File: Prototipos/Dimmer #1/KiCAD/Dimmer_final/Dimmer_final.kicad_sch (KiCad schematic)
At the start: 27 parts, among them J2 Conn_01x02, K1 SRD-05VDC-SL-C, Q1 BC548B, Q2 BT137, U1 MOC3021M, U2 EL817

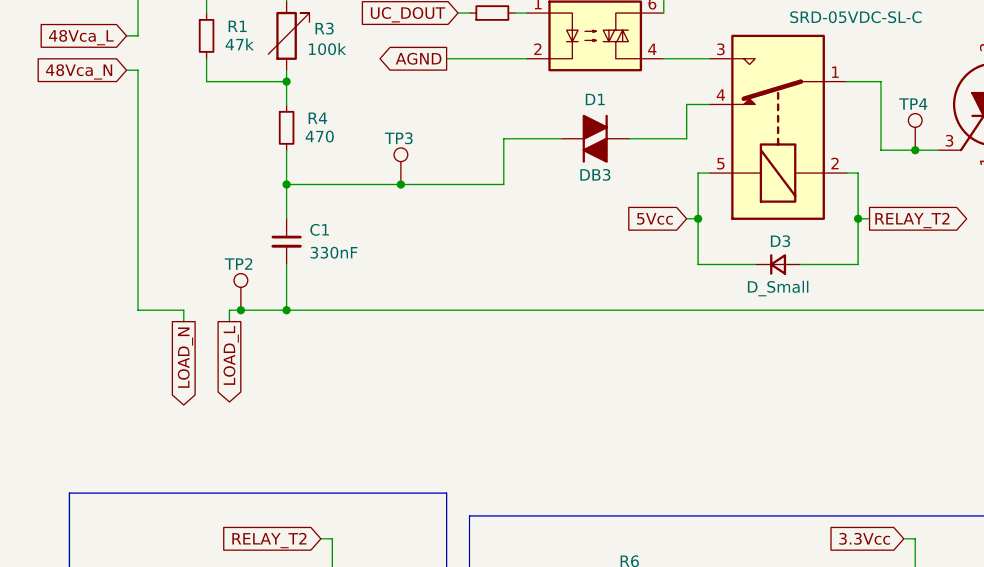
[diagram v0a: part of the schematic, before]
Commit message: Primeras modificaciones para constraints JLCPCB
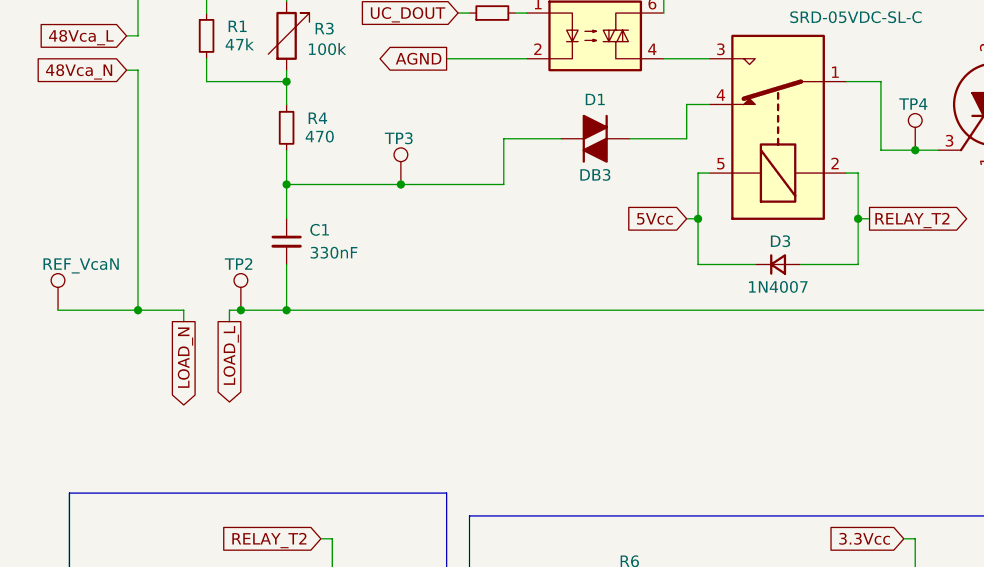
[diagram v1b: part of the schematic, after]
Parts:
- added REF_VcaN: TestPoint, TestPoint:TestPoint_Loop_D1.80mm_Drill1.0mm_Beaded, symbol Connector:TestPoint
- D3: value D_Small -> 1N4007
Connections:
- net 48Vca_N: now also REF_VcaN.1
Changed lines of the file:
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@@
+	)
+	(junction
+		(at 46.99 82.55)
+		(diameter 0)
+		(color 0 0 0 0)
 	)
 	(junction
@@
 	(wire
 		(pts
-			(xy 52.07 82.55) (xy 46.99 82.55)
-		)
-		(stroke
-			(width 0)
-			(type default)
-		)
-	)
-	(wire
-		(pts
 			(xy 58.42 82.55) (xy 63.5 82.55)
 		)
@@
 	(wire
 		(pts
+			(xy 38.1 82.55) (xy 46.99 82.55)
+		)
+		(stroke
+			(width 0)
+			(type default)
+		)
+	)
+	(wire
+		(pts
 			(xy 110.49 59.69) (xy 107.95 59.69)
 		)
@@
 		(pts
 			(xy 63.5 64.8245) (xy 63.5 68.58)
+		)
+		(stroke
+			(width 0)
+			(type default)
+		)
+	)
+	(wire
+		(pts
+			(xy 46.99 82.55) (xy 52.07 82.55)
 		)
 		(stroke
@@
 	)
 	(symbol
+		(lib_id "Connector:TestPoint")
+		(at 38.1 82.55 0)
+		(unit 1)
+		(exclude_from_sim no)
+		(in_bom yes)
+		(on_board yes)
+		(dnp no)
+		(property "Reference" "REF_VcaN"
+			(at 36.322 77.47 0)
+			(effects
+				(font
+					(size 1.27 1.27)
+				)
+				(justify left)
+			)
+		)
+		(property "Value" "TestPoint"
+			(at 31.75 79.502 0)
+			(effects
+				(font
+					(size 1.27 1.27)
+				)
+				(justify left)
+				(hide yes)
+			)
+		)
+		(property "Footprint" "TestPoint:TestPoint_Loop_D1.80mm_Drill1.0mm_Beaded"
+			(at 43.18 82.55 0)
+			(effects
+				(font
+					(size 1.27 1.27)
+				)
+				(hide yes)
+			)
+		)
+		(property "Datasheet" "~"
+			(at 43.18 82.55 0)
+			(effects
+				(font
+					(size 1.27 1.27)
+				)
+				(hide yes)
+			)
+		)
+		(property "Description" "test point"
+			(at 38.1 82.55 0)
+			(effects
+				(font
+					(size 1.27 1.27)
+				)
+				(hide yes)
+			)
+		)
+		(pin "1"
+		)
+		(instances
+			(project "Dimmer_final"
+				(path "/7934e872-2b7f-4f8f-a0b6-741d97320597"
+					(reference "REF_VcaN")
+					(unit 1)
+				)
+			)
+		)
+	)
+	(symbol
 		(lib_id "Device:R_Small")
 		(at 57.15 119.38 90)
@@
 			)
 		)
-		(property "Value" "D_Small"
+		(property "Value" "1N4007"
 			(at 118.11 80.01 0)
 			(effects

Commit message: Reversionado dimmer para fabricación industrial
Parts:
- C1, C2: footprint Capacitor_THT:C_Disc_D10.5mm_W5.0mm_P7.50mm -> Capacitor_THT:C_Disc_D4.7mm_W2.5mm_P5.00mm
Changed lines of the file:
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@@
 			)
 		)
-		(property "Footprint" "Capacitor_THT:C_Disc_D10.5mm_W5.0mm_P7.50mm"
+		(property "Footprint" "Capacitor_THT:C_Disc_D4.7mm_W2.5mm_P5.00mm"
 			(at 63.5 74.93 0)
 			(effects
@@
 			)
 		)
-		(property "Footprint" "Capacitor_THT:C_Disc_D10.5mm_W5.0mm_P7.50mm"
+		(property "Footprint" "Capacitor_THT:C_Disc_D4.7mm_W2.5mm_P5.00mm"
 			(at 154.94 69.85 0)
 			(effects

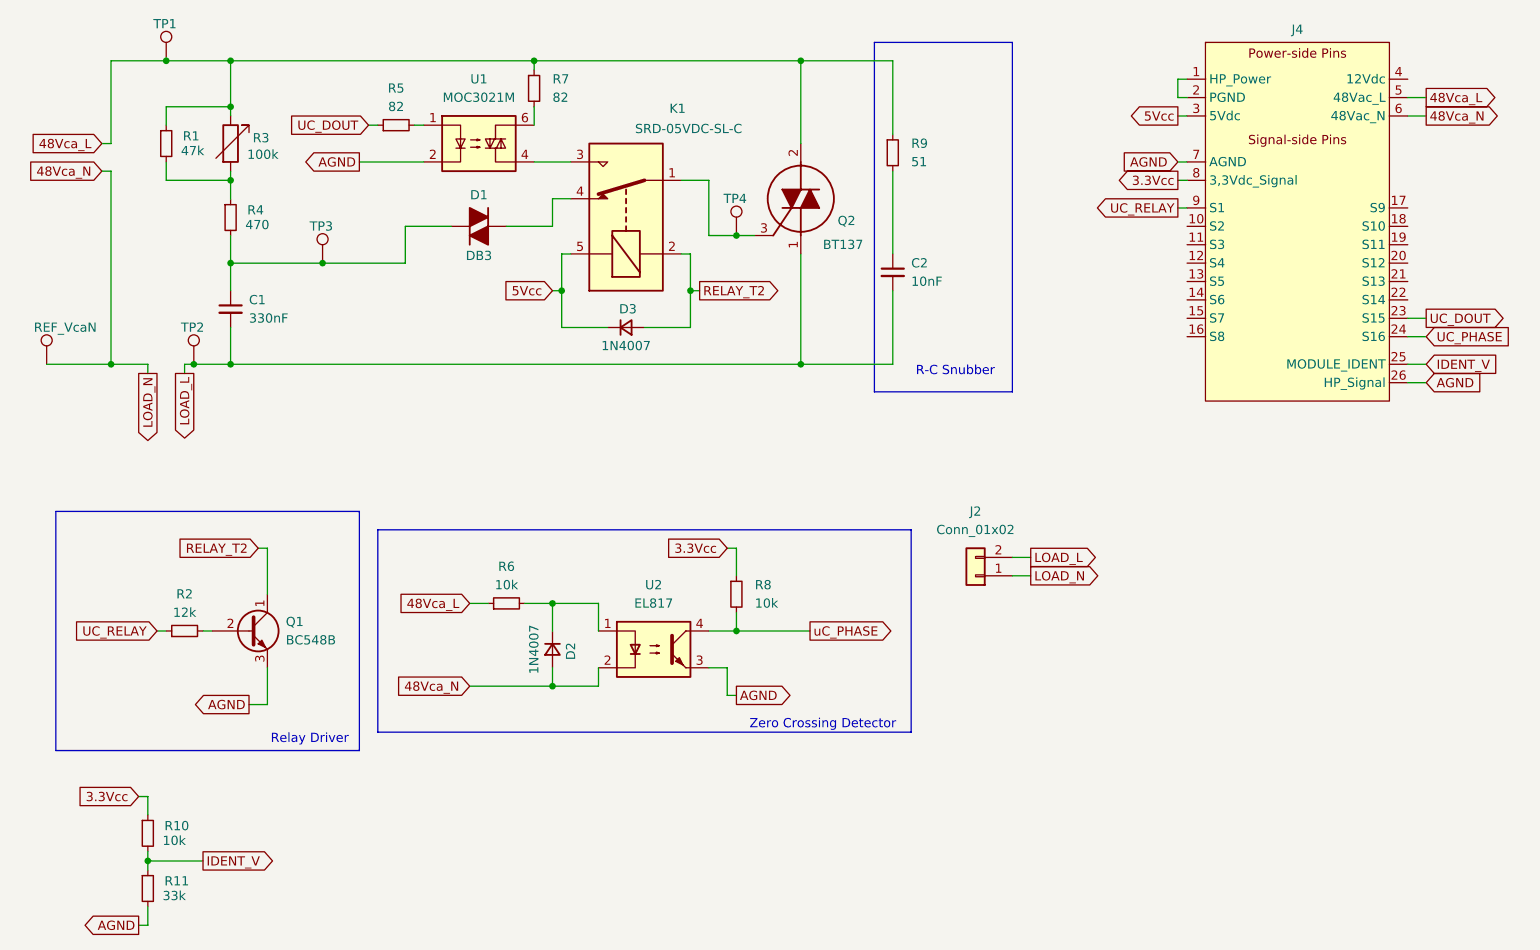
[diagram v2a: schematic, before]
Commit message: Agregar titulo de módulo y firma
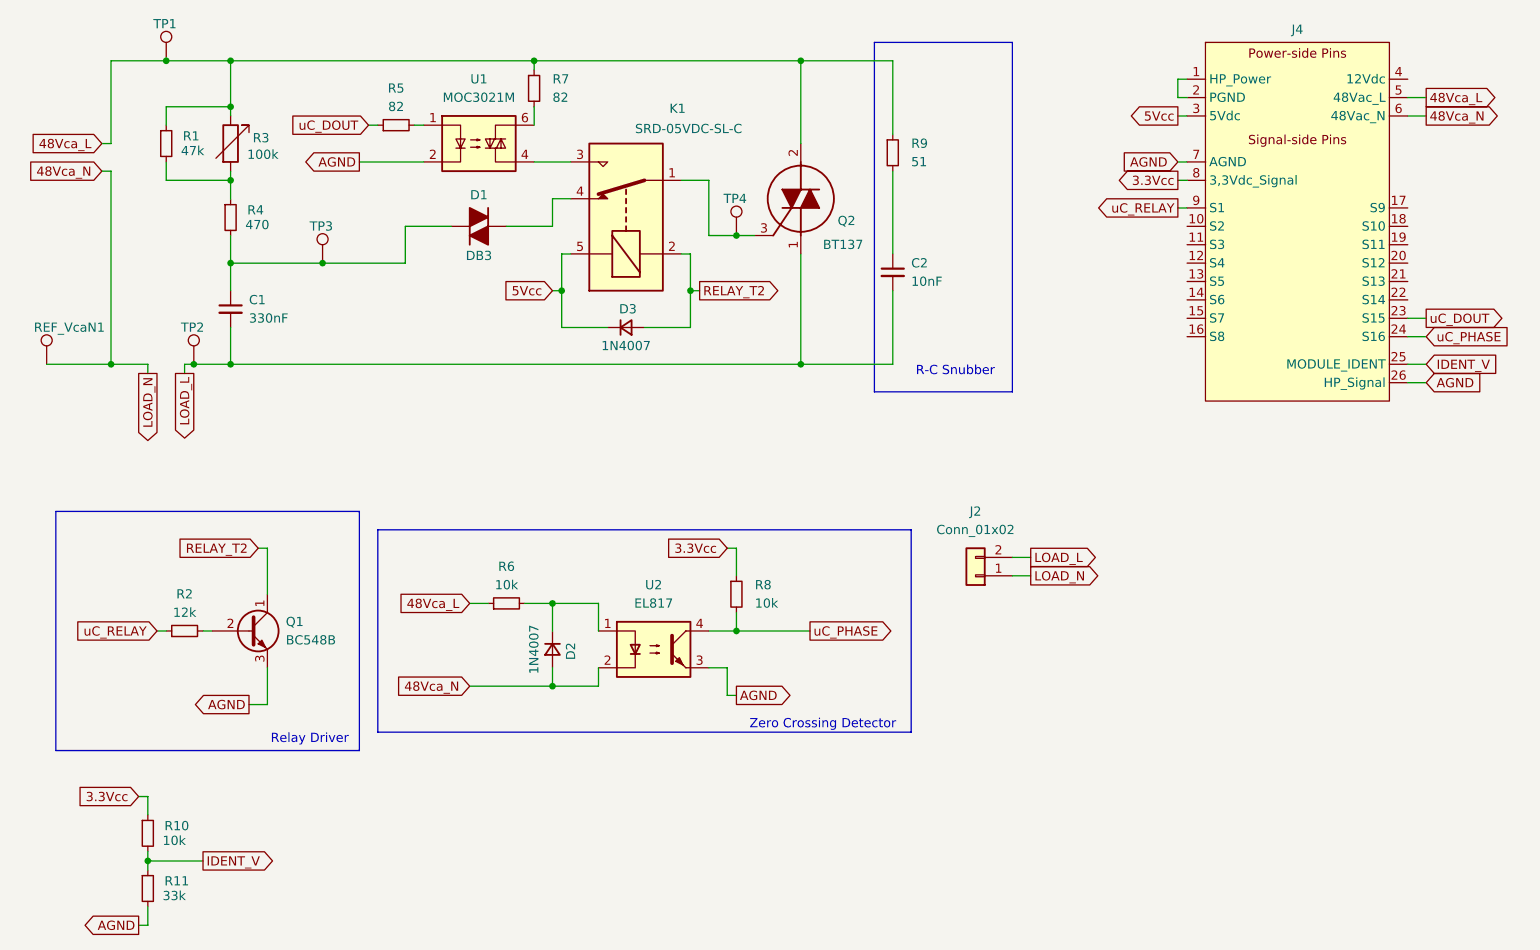
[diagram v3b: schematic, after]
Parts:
- renumbered REF_VcaN to REF_VcaN1
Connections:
- net UC_PHASE is gone; now on net uC_PHASE: J4.24 (S16)
- net UC_DOUT renamed uC_DOUT
- net UC_RELAY renamed uC_RELAY
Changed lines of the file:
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@@
 		)
 	)
-	(global_label "UC_DOUT"
+	(global_label "uC_DOUT"
 		(shape input)
 		(at 82.55 49.53 180)
@@
 		)
 		(property "Intersheetrefs" "${INTERSHEET_REFS}"
-			(at 71.0981 49.53 0)
+			(at 71.2796 49.53 0)
 			(effects
 				(font
@@
 		)
 	)
-	(global_label "UC_RELAY"
+	(global_label "uC_RELAY"
 		(shape output)
 		(at 194.31 60.96 180)
@@
 		)
 		(property "Intersheetrefs" "${INTERSHEET_REFS}"
-			(at 182.1324 60.96 0)
+			(at 182.3139 60.96 0)
 			(effects
 				(font
@@
 		)
 	)
-	(global_label "UC_RELAY"
+	(global_label "uC_RELAY"
 		(shape input)
 		(at 53.34 119.38 180)
@@
 		)
 		(property "Intersheetrefs" "${INTERSHEET_REFS}"
-			(at 41.1624 119.38 0)
+			(at 41.3439 119.38 0)
 			(effects
 				(font
@@
 		)
 	)
-	(global_label "UC_PHASE"
+	(global_label "uC_PHASE"
 		(shape input)
 		(at 228.6 78.74 0)
@@
 		)
 		(property "Intersheetrefs" "${INTERSHEET_REFS}"
-			(at 241.2009 78.74 0)
+			(at 241.0194 78.74 0)
 			(effects
 				(font
@@
 		)
 	)
-	(global_label "UC_DOUT"
+	(global_label "uC_DOUT"
 		(shape output)
 		(at 228.6 76.2 0)
@@
 		)
 		(property "Intersheetrefs" "${INTERSHEET_REFS}"
-			(at 240.0519 76.2 0)
+			(at 239.8704 76.2 0)
 			(effects
 				(font
@@
 		(on_board yes)
 		(dnp no)
-		(property "Reference" "REF_VcaN"
+		(property "Reference" "REF_VcaN1"
 			(at 36.322 77.47 0)
 			(effects
@@
 			(project "Dimmer_final"
 				(path "/7934e872-2b7f-4f8f-a0b6-741d97320597"
-					(reference "REF_VcaN")
-					(unit 1)
-				)
+					(reference "REF_VcaN1")
+					(unit 1)
+				)

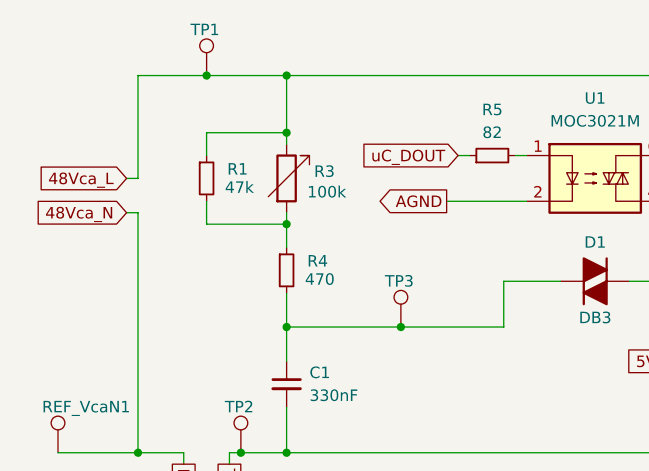
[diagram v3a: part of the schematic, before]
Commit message: Actualizar valor de resistencia R1 a 33k
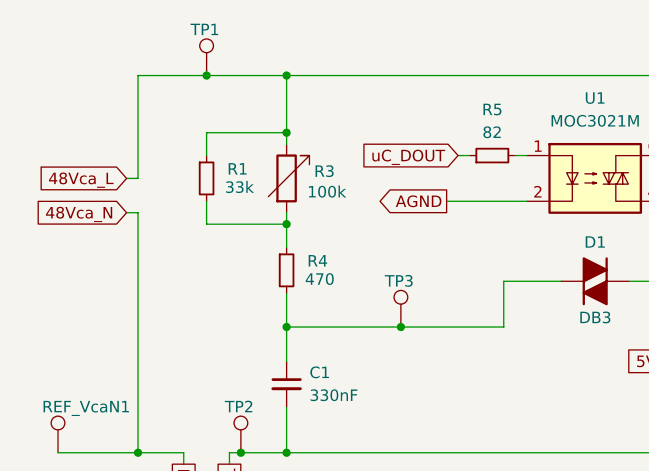
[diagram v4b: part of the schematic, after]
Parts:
- R1: value 47k -> 33k
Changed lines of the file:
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@@
 			)
 		)
-		(property "Value" "47k"
+		(property "Value" "33k"
 			(at 56.642 53.086 0)
 			(effects

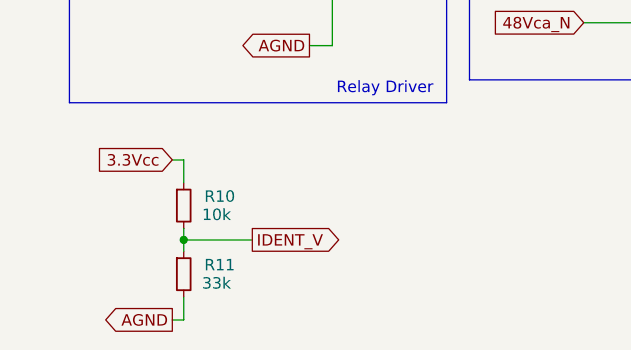
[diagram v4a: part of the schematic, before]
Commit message: Corregir esquemático de Dimmer
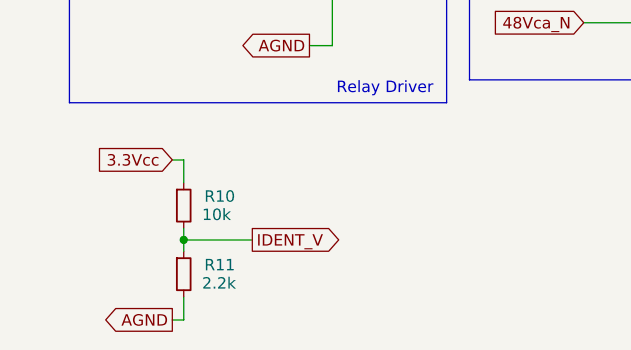
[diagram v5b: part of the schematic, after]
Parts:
- R11: value 33k -> 2.2k
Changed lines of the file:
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@@
 			)
 		)
-		(property "Value" "33k"
+		(property "Value" "2.2k"
 			(at 54.102 155.956 0)
 			(effects
